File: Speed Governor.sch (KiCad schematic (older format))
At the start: 24 parts

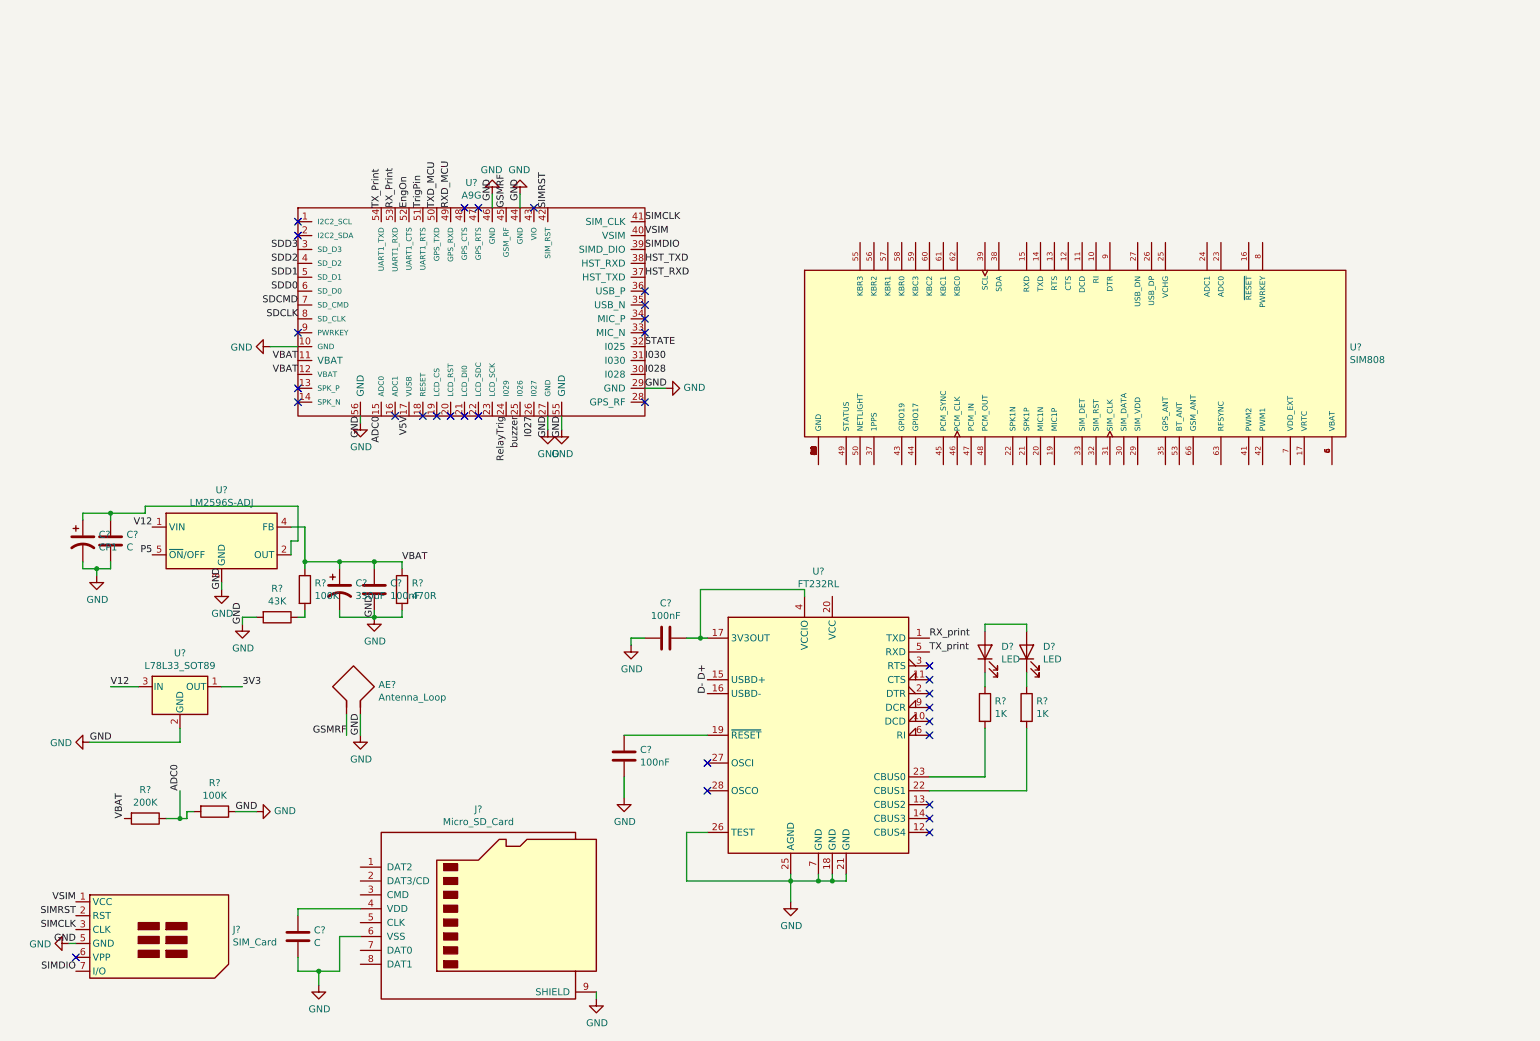
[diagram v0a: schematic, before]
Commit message: completed circuit design, annotated and added power flags
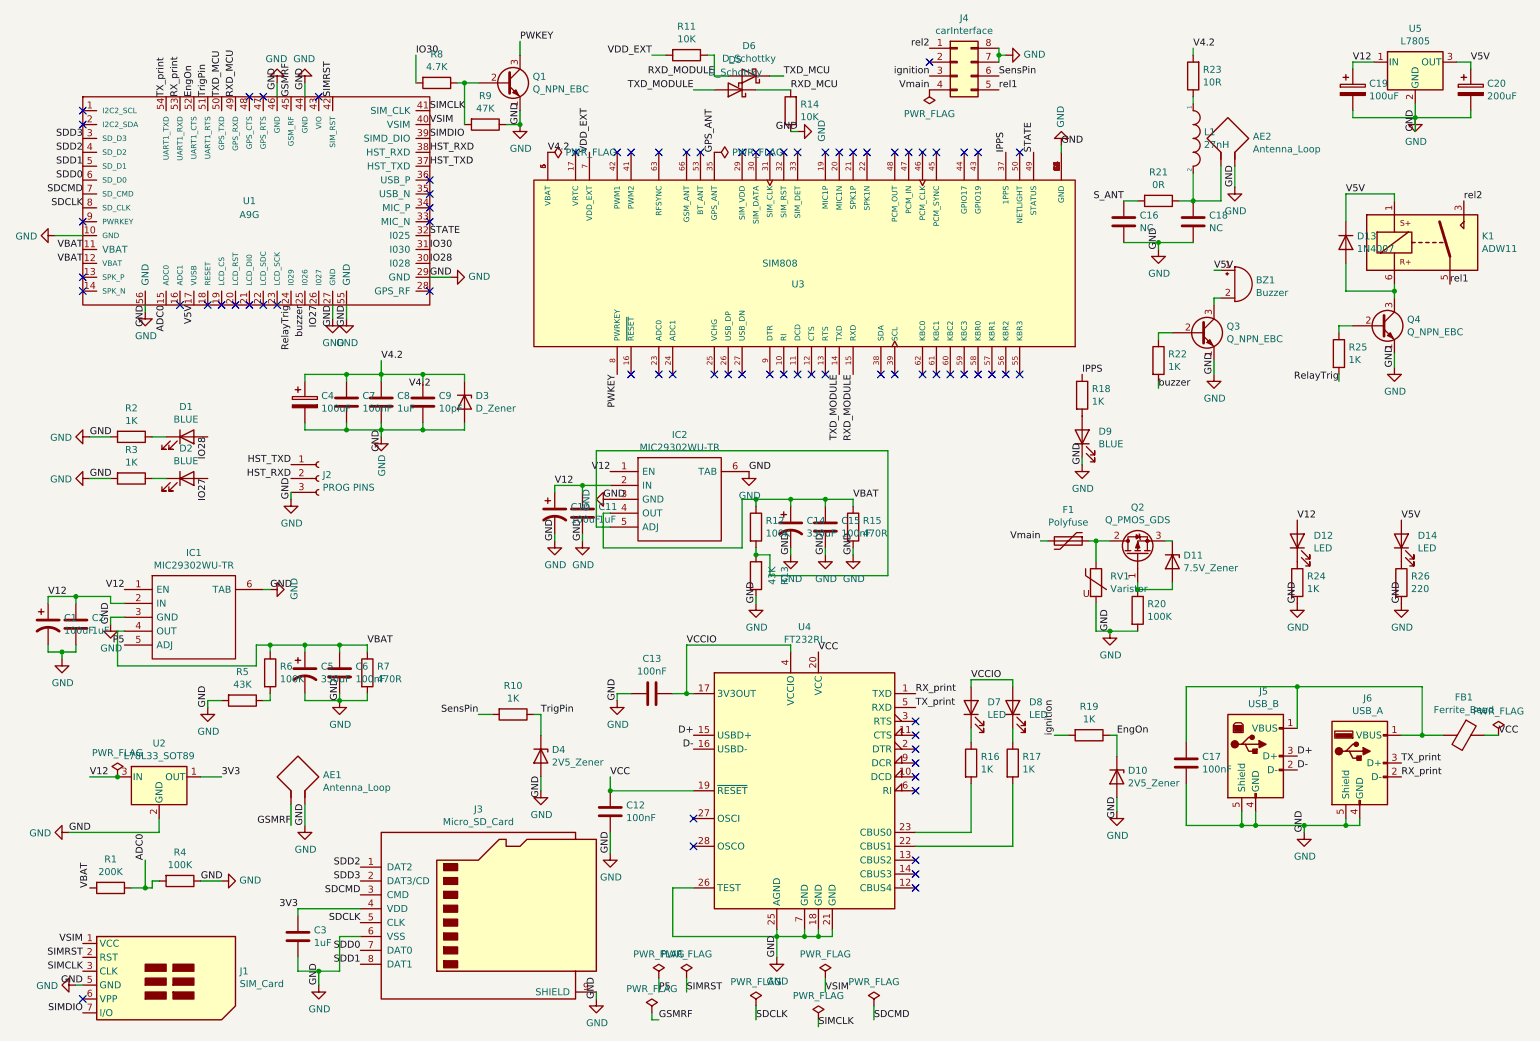
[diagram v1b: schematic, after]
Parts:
- removed U?: LM2596S-ADJ, Package_TO_SOT_SMD:TO-263-5_TabPin3, symbol Regulator_Switching:LM2596S-ADJ
- added AE2: Antenna_Loop, symbol Device:Antenna_Loop
- added BZ1: Buzzer, symbol Device:Buzzer
- added C10: 100uF, symbol Device:CP1
- added C11, C8: 1uF, symbol Device:C
- added C14: 330uF, symbol Device:CP1
- added C15, C17, C7: 100nF, symbol Device:C
- added C16, C18: NC, symbol Device:C
- added C19, C4: 100uF, symbol Device:CP
- added C20: 200uF, symbol Device:CP
- added C9: 10pF, symbol Device:C
- added D1, D2, D9: BLUE, symbol Device:LED
- added D10, D4: 2V5_Zener, symbol Device:D_Zener
- added D11: 7.5V_Zener, symbol Device:D_Zener
- added D12, D14: LED, symbol Device:LED
- added D13: 1N4007, symbol Device:D
- added D3: D_Zener, symbol Device:D_Zener
- added D5, D6: D_Schottky, symbol Device:D_Schottky
- added F1: Polyfuse, symbol Device:Polyfuse
- added FB1: Ferrite_Bead, symbol Device:Ferrite_Bead
- added IC1, IC2: MIC29302WU-TR, MIC29302WUTR, symbol MIC29302WU-TR:MIC29302WU-TR
- added J2: PROG PINS, symbol Connector:Conn_01x03_Female
- added J4: carInterface, symbol Connector_Generic:Conn_02x04_Counter_Clockwise
- added J5: USB_B, symbol Connector:USB_B
- added J6: USB_A, symbol Connector:USB_A
- added K1: ADW11, Relay_THT:Relay_1P1T_NO_10x24x18.8mm_Panasonic_ADW11xxxxW_THT, symbol Relay:ADW11
- added L1: 27nH, symbol pspice:INDUCTOR
- added Q1, Q3, Q4: Q_NPN_EBC, symbol Device:Q_NPN_EBC
- added Q2: Q_PMOS_GDS, symbol Device:Q_PMOS_GDS
- added R10, R18, R19, R2, R22, R24, R25, R3: 1K, symbol Device:R
- added R11, R14: 10K, symbol Device:R
- added R12, R20: 100K, symbol Device:R
- added R13: 43K, symbol Device:R
- added R15: 470R, symbol Device:R
- added R21: 0R, symbol Device:R
- added R23: 10R, symbol Device:R
- added R26: 220, symbol Device:R
- added R8: 4.7K, symbol Device:R
- added R9: 47K, symbol Device:R
- added RV1: Varistor, symbol Device:Varistor
- added U5: L7805, symbol Regulator_Linear:L7805
- C1: renamed from C?; value CP1 -> 100uF
- C2, C3: renamed from C?; value C -> 1uF
- gave numbers to parts that had none: 20
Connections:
- net RX_Print is gone; now on net RX_print: U1.53 (UART1_RXD)
- net TX_Print is gone; now on net TX_print: U1.54 (UART1_TXD)
- net 3V3: now also C3.1, J3.4 (VDD)
- net D+: now also J5.3 (D+)
- net D-: now also J5.2 (D-)
- net EngOn: now also D10.1 (K), R19.1
- net GND: now also U3.1 (GND), U3.18 (GND), U3.2 (GND), U3.28 (GND), U3.3 (GND), U3.34 (GND), U3.36 (GND), U3.40 (GND), U3.51 (GND), U3.52 (GND), U3.54 (GND), U3.64 (GND), U3.65 (GND), U3.67 (GND), U3.68 (GND), AE2.2, C10.2, C11.2, C14.2, C15.2, C16.2, C17.2, C18.2, C19.2, C20.2, C4.2, C7.2, C8.2, C9.2, D10.2 (A), D3.2 (A), D4.2 (A), D9.1 (K), IC1.3 (GND), IC1.6 (TAB), IC2.3 (GND), IC2.6 (TAB), J2.3 (Pin_3), J4.7 (Pin_7), J4.8 (Pin_8), J5.4 (GND), J5.5 (Shield), J6.4 (GND), J6.5 (Shield), Q1.1 (E), Q3.1 (E), Q4.1 (E), R13.1, R14.1, R15.2, R2.2, R20.2, R24.2, R26.2, R3.2, R9.1, RV1.2, U5.2 (GND)
- net HST_RXD: now also U1.38 (HST_RXD), J2.2 (Pin_2); no longer U1.37 (HST_TXD)
- net HST_TXD: now also U1.37 (HST_TXD), J2.1 (Pin_1); no longer U1.38 (HST_RXD)
- net P5: now also IC1.5 (ADJ)
- net RXD_MCU: now also D5.1 (K), R14.2
- net RX_print: now also J6.2 (D-)
- net RelayTrig: now also R25.2
- net SDCLK: now also J3.5 (CLK)
- net SDCMD: now also J3.3 (CMD)
- net SDD0: now also J3.7 (DAT0)
- net SDD1: now also J3.8 (DAT1)
- net SDD2: now also J3.1 (DAT2)
- net SDD3: now also J3.2 (DAT3/CD)
- net STATE: now also U3.49 (STATUS)
- net TXD_MCU: now also D6.1 (K)
- net TX_print: now also J6.3 (D+)
- net TrigPin: now also D4.1 (K), R10.1
- net V12: now also C1.1, C2.1, C10.1, C11.1, C19.1, D12.2 (A), IC1.1 (EN), IC1.2 (IN), IC2.1 (EN), IC2.2 (IN), U5.1 (IN)
- net V5V: now also BZ1.1 (-), C20.1, D13.1 (K), D14.2 (A), K1.1, U5.3 (OUT)
- net VBAT: now also C14.1, C15.1, IC1.4 (OUT), IC2.4 (OUT), R12.1, R15.1
- net buzzer: now also R22.2
- net VCCIO: now reaches C13.1, U4.17 (3V3OUT), U4.4 (VCCIO)
- net VCCIO: now also D7.2 (A), D8.2 (A)
- net VCC: now reaches C12.1, U4.19 (~RESET~)
- net VCC: now also U4.20 (VCC), FB1.1
- net TXD_MODULE: now reaches U3.14 (TXD)
- net TXD_MODULE: now also D5.2 (A)
- net RXD_MODULE: now reaches U3.15 (RXD)
- net RXD_MODULE: now also D6.2 (A), R11.1
- net GPS_ANT: now reaches U3.35 (GPS_ANT)
- net IPPS: now reaches U3.37 (1PPS)
- net IPPS: now also R18.1
- net V4.2: now reaches U3.4 (VBAT), U3.5 (VBAT), U3.6 (VBAT)
- net V4.2: now also C4.1, C7.1, C8.1, C9.1, D3.1 (K), R23.2
- net VDD_EXT: now reaches U3.7 (VDD_EXT)
- net VDD_EXT: now also R11.2
- net PWKEY: now reaches U3.8 (PWRKEY)
- net PWKEY: now also Q1.3 (C)
- net I027 renamed IO27
- net IO27: now also D2.2 (A)
- net I028 renamed IO28
- net IO28: now also D1.2 (A)
- net I030 renamed IO30
- net IO30: now also R8.2
- new net: Q1.2 (B), R8.1, R9.2
- new net: D1.1 (K), R2.1
- new net: D2.1 (K), R3.1
- new net: IC2.5 (ADJ), R12.2, R13.2
- new net: L1.1, R23.1
- new net: AE2.1, C18.1, L1.2, R21.1
- new net: C17.1, FB1.2, J5.1 (VBUS), J6.1 (VBUS)
- new net: D13.2 (A), K1.6, Q4.3 (C)
- new net: Q4.2 (B), R25.1
- new net: Q3.2 (B), R22.1
- new net: BZ1.2 (+), Q3.3 (C)
- new net: D11.2 (A), Q2.1 (G), R20.1
- new net: F1.1, Q2.2 (D), RV1.1
- new net: D11.1 (K), Q2.3 (S)
- new net: D12.1 (K), R24.1
- new net: D14.1 (K), R26.1
- new net: D9.2 (A), R18.2
- new net S_ANT: C16.1, R21.2
- new net SensPin: J4.6 (Pin_6), R10.2
- new net Vmain: F1.2, J4.4 (Pin_4)
- new net ignition: J4.3 (Pin_3), R19.2
- new net rel1: J4.5 (Pin_5), K1.5
- new net rel2: J4.1 (Pin_1), K1.3
- no-connect marks 31 -> 76
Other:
- moved on the sheet: AE1, C1, C12, C13, C2, C5, C6, D7, D8, J1, R1, R16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
